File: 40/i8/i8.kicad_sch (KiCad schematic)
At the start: 133 parts, among them J1 ZX-SH1.0-4PWT, J2 Conn_DEBUG, SW1 MX_SW, SW10 MX_SW, SW11 MX_SW, SW12 MX_SW, SW13 MX_SW, SW14 MX_SW, SW15 MX_SW, SW16 MX_SW, SW17 MX_SW, SW18 MX_SW, SW19 MX_SW, SW2 MX_SW, SW20 MX_SW, SW21 MX_SW, SW22 MX_SW, SW23 MX_SW, SW24 MX_SW, SW25 MX_SW, SW26 MX_SW, SW27 MX_SW, SW28 MX_SW, SW29 MX_SW, SW3 MX_SW, SW30 MX_SW, SW31 MX_SW, SW32 MX_SW, SW33 MX_SW, SW34 MX_SW, SW35 MX_SW, SW36 MX_SW, SW37 MX_SW, SW38 MX_SW, SW39 MX_SW, SW4 MX_SW, SW40 MX_SW, SW41 MX_SW, SW42 MX_SW, SW43 MX_SW, SW44 MX_SW, SW45 MX_SW, SW46 MX_SW, SW47 MX_SW, SW48 MX_SW, SW49 MX_SW, SW5 MX_SW, SW50 MX_SW, SW6 MX_SW, SW7 MX_SW, SW8 MX_SW, SW9 MX_SW, U1 XC6206P332MR-G, U2 RP2040, U3 W25Q16JVUXIQ, Y1 Crystal_GND24

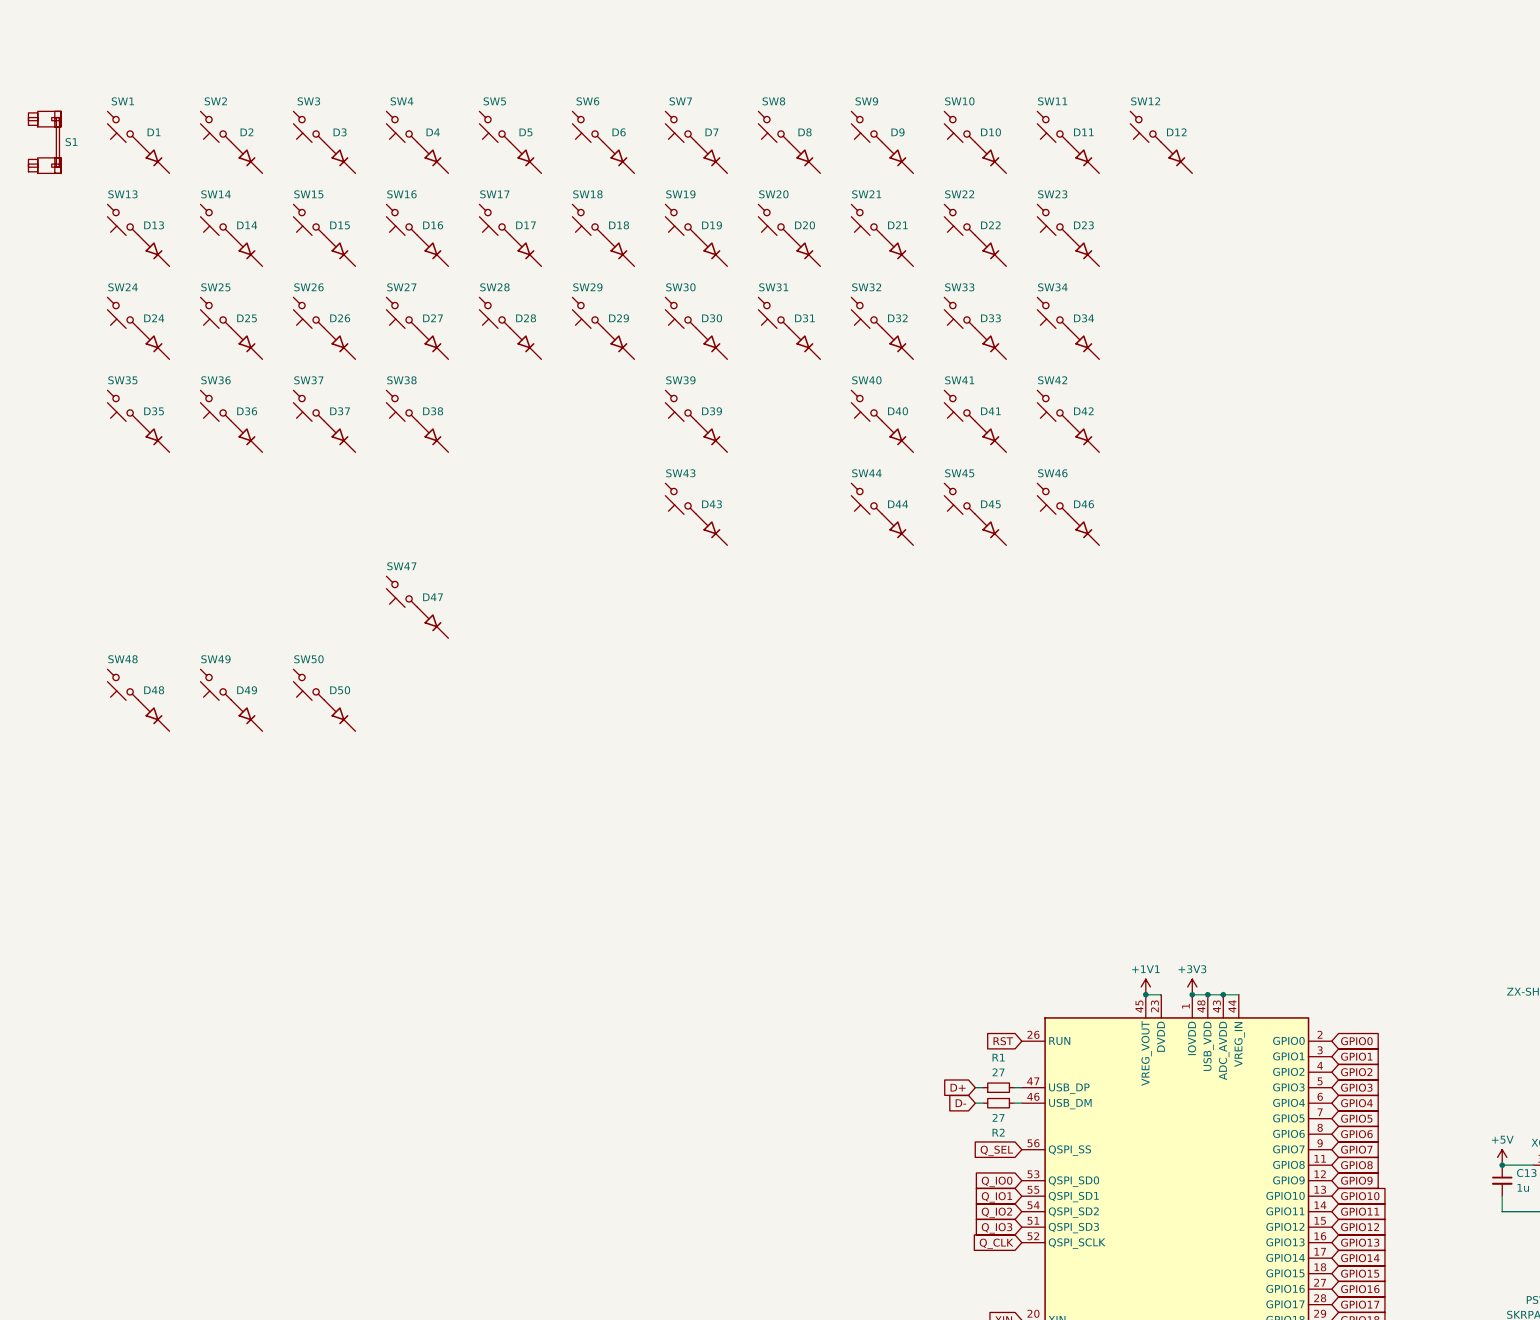
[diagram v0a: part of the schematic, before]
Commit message: tako40_i8 drafted
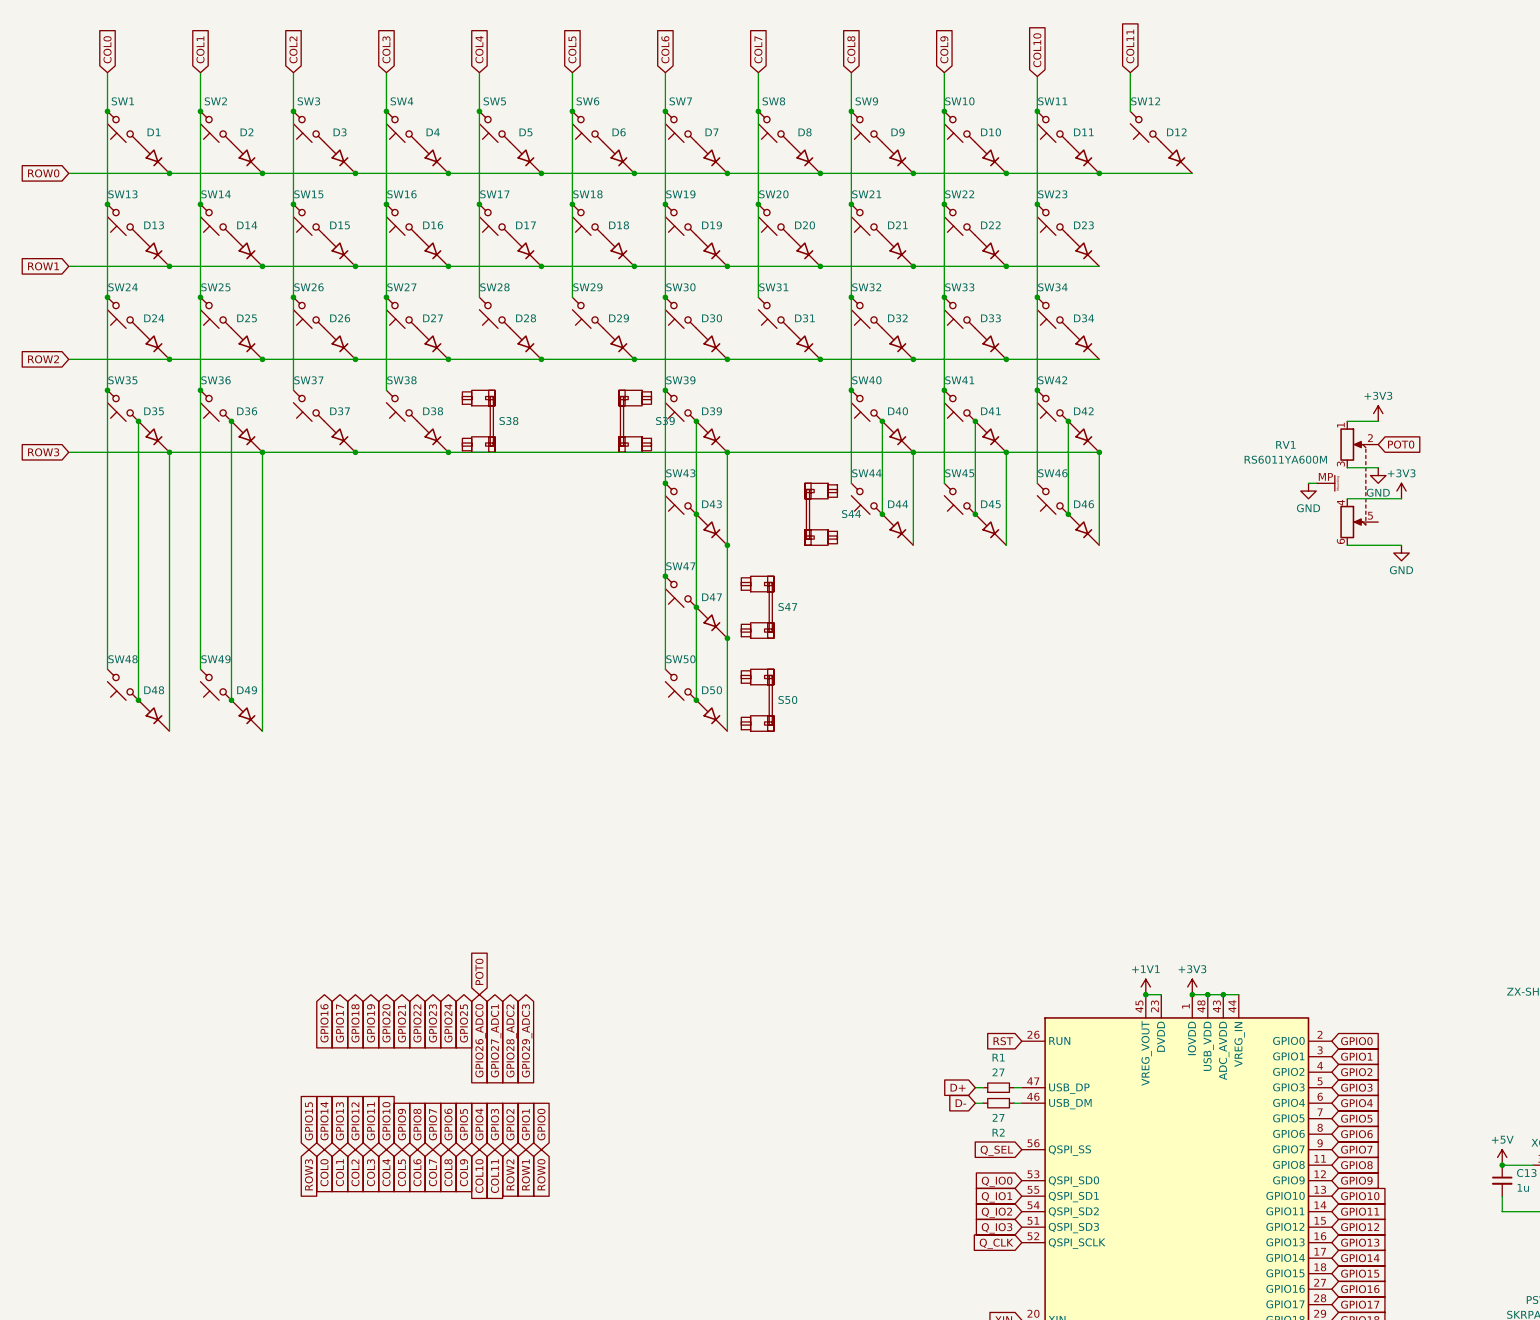
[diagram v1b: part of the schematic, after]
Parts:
- added RV1: RS6011YA600M, shoonies_parts:RS6011YA600M, symbol Device:R_Potentiometer_Dual_MountingPin
- added S39, S44: MX_S, PCM_marbastlib-mx:STAB_MX_P_2u, symbol PCM_marbastlib-mx:MX_stab
- added S47: MX_S, PCM_marbastlib-mx:STAB_MX_P_6.25u, symbol PCM_marbastlib-mx:MX_stab
- added S50: MX_S, PCM_marbastlib-mx:STAB_MX_P_7u, symbol PCM_marbastlib-mx:MX_stab
- renumbered S1 to S38
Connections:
- net GPIO10 is gone; now on net COL4: U2.13 (GPIO10)
- net GPIO11 is gone; now on net COL3: U2.14 (GPIO11)
- net GPIO12 is gone; now on net COL2: U2.15 (GPIO12)
- net GPIO13 is gone; now on net COL1: U2.16 (GPIO13)
- net GPIO14 is gone; now on net COL0: U2.17 (GPIO14)
- net GPIO3 is gone; now on net COL11: U2.5 (GPIO3)
- net GPIO4 is gone; now on net COL10: U2.6 (GPIO4)
- net GPIO5 is gone; now on net COL9: U2.7 (GPIO5)
- net GPIO6 is gone; now on net COL8: U2.8 (GPIO6)
- net GPIO7 is gone; now on net COL7: U2.9 (GPIO7)
- net GPIO8 is gone; now on net COL6: U2.11 (GPIO8)
- net GPIO9 is gone; now on net COL5: U2.12 (GPIO9)
- net +3V3: now also RV1.1, RV1.4
- net GND: now also RV1.3, RV1.6, RV1.MP (MountPin)
- net GPIO0: now also D1.1 (K), D10.1 (K), D11.1 (K), D12.1 (K), D2.1 (K), D3.1 (K), D4.1 (K), D5.1 (K), D6.1 (K), D7.1 (K), D8.1 (K), D9.1 (K)
- net GPIO1: now also D13.1 (K), D14.1 (K), D15.1 (K), D16.1 (K), D17.1 (K), D18.1 (K), D19.1 (K), D20.1 (K), D21.1 (K), D22.1 (K), D23.1 (K)
- net GPIO15: now also D35.1 (K), D36.1 (K), D37.1 (K), D38.1 (K), D39.1 (K), D40.1 (K), D41.1 (K), D42.1 (K), D43.1 (K), D44.1 (K), D45.1 (K), D46.1 (K), D47.1 (K), D48.1 (K), D49.1 (K), D50.1 (K)
- net GPIO2: now also D24.1 (K), D25.1 (K), D26.1 (K), D27.1 (K), D28.1 (K), D29.1 (K), D30.1 (K), D31.1 (K), D32.1 (K), D33.1 (K), D34.1 (K)
- net GPIO26_ADC0: now also RV1.2
- net COL8: now reaches SW32.2
- net COL8: now also SW21.2, SW40.2, SW44.2, SW9.2
- net at D40.2 (A), SW40.1: now also D44.2 (A), SW44.1
- net at D35.2 (A), SW35.1: now also D48.2 (A), SW48.1
- net COL0: now reaches SW35.2
- net COL0: now also SW1.2, SW13.2, SW24.2, SW48.2
- net COL4: now reaches SW17.2
- net COL4: now also SW28.2, SW5.2
- net COL3: now reaches SW16.2
- net COL3: now also SW27.2, SW38.2, SW4.2
- net at D45.2 (A), SW45.1: now also D41.2 (A), SW41.1
- net COL9: now reaches SW45.2
- net COL9: now also SW10.2, SW22.2, SW33.2, SW41.2
- net COL10: now reaches SW34.2
- net COL10: now also SW11.2, SW23.2, SW42.2, SW46.2
- net COL6: now reaches SW7.2
- net COL6: now also SW19.2, SW30.2, SW39.2, SW43.2, SW47.2, SW50.2
- net COL1: now reaches SW14.2
- net COL1: now also SW2.2, SW25.2, SW36.2, SW49.2
- net at D43.2 (A), SW43.1: now also D39.2 (A), D47.2 (A), D50.2 (A), SW39.1, SW47.1, SW50.1
- net COL5: now reaches SW29.2
- net COL5: now also SW18.2, SW6.2
- net COL2: now reaches SW37.2
- net COL2: now also SW15.2, SW26.2, SW3.2
- net COL7: now reaches SW31.2
- net COL7: now also SW20.2, SW8.2
- net at D46.2 (A), SW46.1: now also D42.2 (A), SW42.1
- net at D49.2 (A), SW49.1: now also D36.2 (A), SW36.1
- net COL11: now reaches SW12.2
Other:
- moved on the sheet: D47, D50, S38, SW47, SW50

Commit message: i8 iterating
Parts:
- SW1, SW10, SW11, SW12, SW13, SW14, SW15, SW16, SW17, SW18, SW19, SW2, SW20, SW21, SW22, SW23, SW24, SW25, SW26, SW27, SW28, SW29, SW3, SW30, SW31, SW32, SW33, SW34, SW35, SW36, SW37, SW38, SW39, SW4, SW40, SW41, SW42, SW43, SW44, SW45, SW46, SW47, SW48, SW49, SW5, SW50, SW6, SW7, SW8, SW9: footprint PCM_marbastlib-mx:SW_MX_HS_S_CPG151101S11_1u -> PCM_marbastlib-mx:SW_MX_1u
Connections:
- net COL0: now also U2.15 (GPIO12); no longer U2.17 (GPIO14)
- net COL1: now also U2.14 (GPIO11); no longer U2.16 (GPIO13)
- net COL10: now also U2.4 (GPIO2); no longer U2.6 (GPIO4)
- net COL11: now also U2.3 (GPIO1); no longer U2.5 (GPIO3)
- net COL2: now also U2.13 (GPIO10); no longer U2.15 (GPIO12)
- net COL3: now also U2.12 (GPIO9); no longer U2.14 (GPIO11)
- net COL4: now also U2.11 (GPIO8); no longer U2.13 (GPIO10)
- net COL5: now also U2.9 (GPIO7); no longer U2.12 (GPIO9)
- net COL6: now also U2.8 (GPIO6); no longer U2.11 (GPIO8)
- net COL7: now also U2.7 (GPIO5); no longer U2.9 (GPIO7)
- net COL8: now also U2.6 (GPIO4); no longer U2.8 (GPIO6)
- net COL9: now also U2.5 (GPIO3); no longer U2.7 (GPIO5)
- net GPIO0: now also D13.1 (K), D14.1 (K), D15.1 (K), D16.1 (K), D17.1 (K), D18.1 (K), D19.1 (K), D20.1 (K), D21.1 (K), D22.1 (K), D23.1 (K); no longer D1.1 (K), D10.1 (K), D11.1 (K), D12.1 (K), D2.1 (K), D3.1 (K), D4.1 (K), D5.1 (K), D6.1 (K), D7.1 (K), D8.1 (K), D9.1 (K)
- net GPIO15: no longer D35.1 (K), D36.1 (K), D37.1 (K), D38.1 (K), D39.1 (K), D40.1 (K), D41.1 (K), D42.1 (K), D43.1 (K), D44.1 (K), D45.1 (K), D46.1 (K), D47.1 (K), D48.1 (K), D49.1 (K), D50.1 (K)
- net GPIO25: now also D1.1 (K), D10.1 (K), D11.1 (K), D12.1 (K), D2.1 (K), D3.1 (K), D4.1 (K), D5.1 (K), D6.1 (K), D7.1 (K), D8.1 (K), D9.1 (K)
- removed net GPIO1: D13.1 (K), D14.1 (K), D15.1 (K), D16.1 (K), D17.1 (K), D18.1 (K), D19.1 (K), D20.1 (K), D21.1 (K), D22.1 (K), D23.1 (K), U2.3 (GPIO1)
- net GPIO2 renamed GPIO13
- net GPIO13: now also U2.16 (GPIO13); no longer U2.4 (GPIO2)
- new net GPIO14: D35.1 (K), D36.1 (K), D37.1 (K), D38.1 (K), D39.1 (K), D40.1 (K), D41.1 (K), D42.1 (K), D43.1 (K), D44.1 (K), D45.1 (K), D46.1 (K), D47.1 (K), D48.1 (K), D49.1 (K), D50.1 (K), U2.17 (GPIO14)
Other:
- moved on the sheet: D1, D10, D11, D12, D13, D14, D15, D16, D17, D18, D19, D2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
